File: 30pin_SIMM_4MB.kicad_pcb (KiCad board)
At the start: 2 copper layers, 88.9 x 20 mm, 10 parts, among them IC1 4Mx4bit_DRAM, IC2 4Mx4bit_DRAM, IC3 4Mx1bit_DRAM, J1 30pin_SIMM_Edge

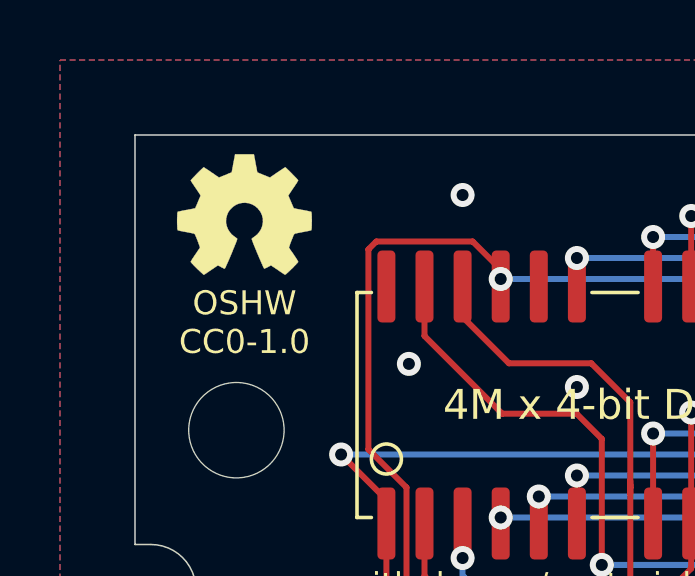
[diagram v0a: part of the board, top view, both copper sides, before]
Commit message: Moved OSHW silkscreen to backside
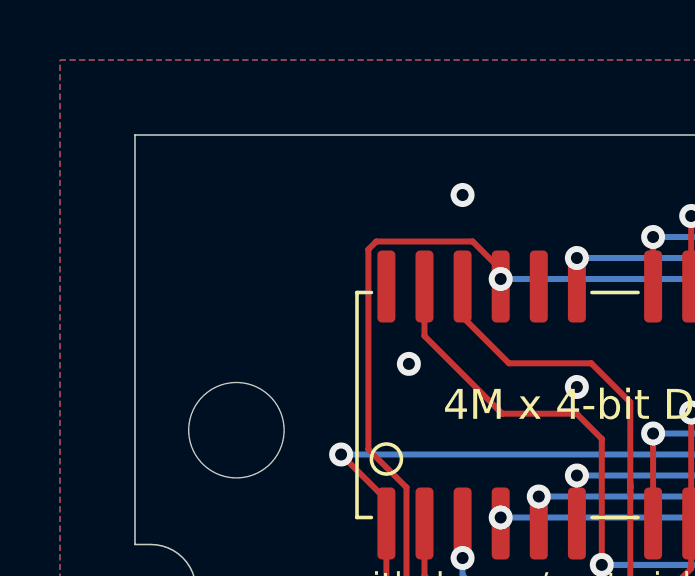
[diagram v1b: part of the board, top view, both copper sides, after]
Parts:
- REF**: moved to B.Cu
- moved REF** 0.27 mm to (103.4, 82.8), turned to 180 degrees

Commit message: Updated gerber files
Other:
- board text added: "30 pin SIMM : 4 MB"
- board text added: "Parity"
- board text removed: "30 pin SIMM 4 MB + Parity"
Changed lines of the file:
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@@
   (general
     (thickness 1.6)
-    (drawings 14)
+    (drawings 15)
     (tracks 313)
     (zones 0)
@@
     )
   )
-  (gr_text JLCJLCJLCJLC (at 171.46 90.55) (layer F.SilkS)
+  (gr_poly (pts (xy 182 96) (xy 177.25 96) (xy 177.25 92.75) (xy 182 92.75)) (layer B.SilkS) (width 0.1))
+  (gr_text ns (at 171 94.5) (layer B.SilkS)
+    (effects (font (size 2.5 2.5) (thickness 0.2)) (justify right mirror))
+  )
+  (gr_text Parity (at 170 87) (layer F.SilkS)
+    (effects (font (size 1 1) (thickness 0.15)))
+  )
+  (gr_text JLCJLCJLCJLC (at 144.46 90.55) (layer F.SilkS)
     (effects (font (size 1 1) (thickness 0.15)))
   )
@@
     (effects (font (size 0.8 0.8) (thickness 0.15)) (justify right))
   )
-  (gr_text ns (at 131.45 84) (layer B.SilkS)
-    (effects (font (size 2 2) (thickness 0.2)) (justify mirror))
-  )
-  (gr_poly (pts (xy 137.86 85.17) (xy 134.26 85.17) (xy 134.26 82.72) (xy 137.86 82.72)) (layer B.SilkS) (width 0.1))
-  (gr_text "30 pin SIMM 4 MB + Parity" (at 160.95 84) (layer B.SilkS)
-    (effects (font (size 2 2) (thickness 0.2)) (justify mirror))
+  (gr_text "30 pin SIMM : 4 MB" (at 144.45 84) (layer B.SilkS)
+    (effects (font (size 3 3) (thickness 0.25)) (justify mirror))
   )
   (gr_line (start 100 93.65) (end 100.53 93.65) (layer Edge.Cuts) (width 0.05))

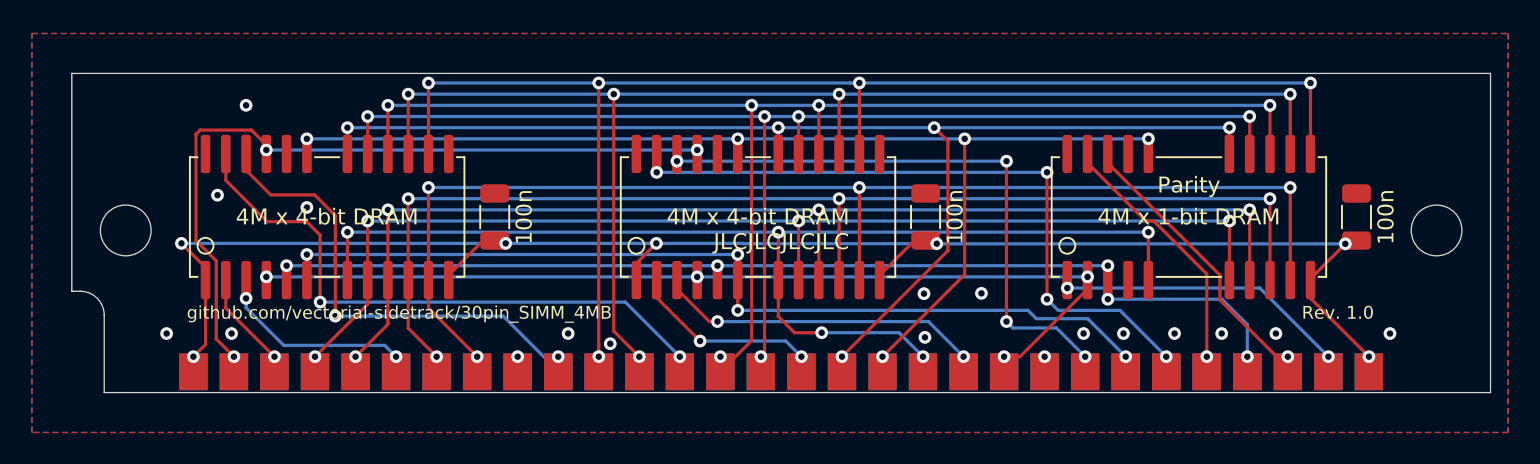
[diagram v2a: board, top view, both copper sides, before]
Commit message: Increased bottom edge clearance by 0.1 mm to 0.25 mm
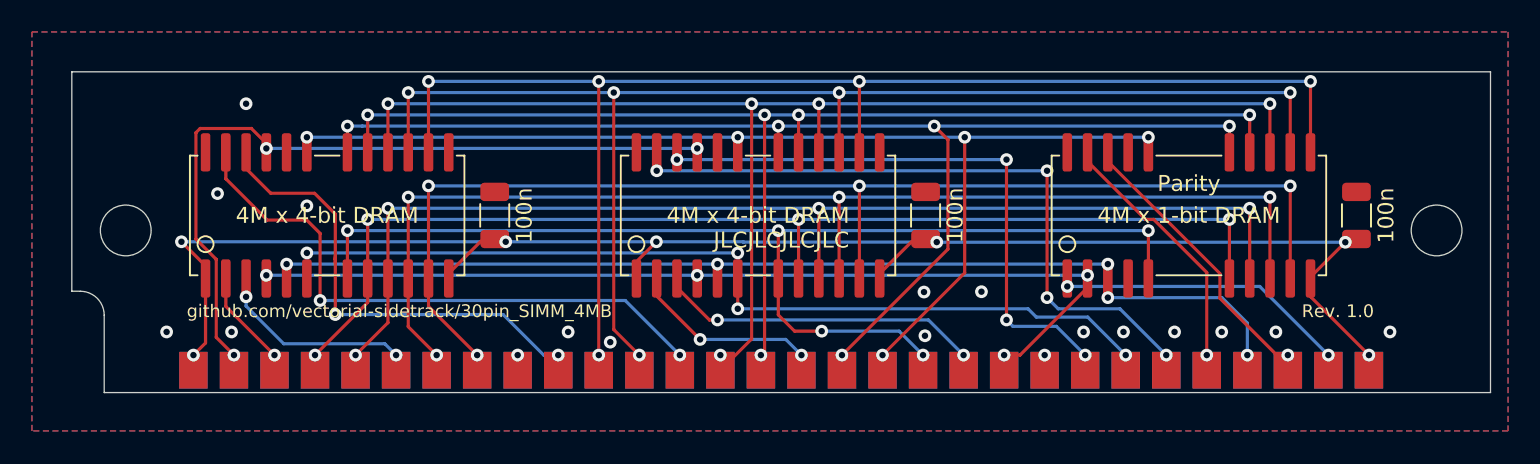
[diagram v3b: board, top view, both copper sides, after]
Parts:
- moved C1 0.10 mm to (126.5, 88.9)
- moved C2 0.10 mm to (153.5, 88.9)
- moved C3 0.10 mm to (180.5, 88.9)
- moved IC1 0.10 mm to (116.0, 88.9)
- moved IC2 0.10 mm to (143.0, 88.9)
- moved IC3 0.10 mm to (170.0, 88.9)
- moved REF** 0.10 mm to (103.4, 82.8)
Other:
- board size 88.9 x 20 mm -> 88.9 x 20.1 mm
